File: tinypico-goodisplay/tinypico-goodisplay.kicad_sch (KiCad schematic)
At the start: 23 parts, among them Q1 Si1308, U1 TinypicoESP32_Symbol

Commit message: Update C4
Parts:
- U2: value (none) -> FPCConn; footprint (none) -> footprint:Hirose_FH12-24S-0.5SH_1x24-1MP_P0.50mm_Horizontal
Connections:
- net GND: no longer U2.MP (26)
- net VCOM: now reaches C1.2, U2.1 (24)
- net VCOM: now also U1.5 (IO4)
- no-connect marks 11 -> 12
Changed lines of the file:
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@@
   (junction (at 60.96 101.6) (diameter 0) (color 0 0 0 0)
   )
+  (junction (at 59.69 99.06) (diameter 0) (color 0 0 0 0)
+  )
   (junction (at 77.47 80.01) (diameter 0) (color 0 0 0 0)
   )
@@
   (junction (at 82.55 87.63) (diameter 0) (color 0 0 0 0)
   )
-  (no_connect (at 227.33 95.25))
+  (no_connect (at 52.07 96.52))
   (no_connect (at 199.39 95.25))
   (no_connect (at 227.33 110.49))
   (no_connect (at 199.39 99.06))
+  (no_connect (at 49.53 160.02))
   (no_connect (at 227.33 80.01))
   (no_connect (at 227.33 102.87))
@@
     (stroke (width 0) (type default) (color 0 0 0 0))
   )
-  (wire (pts (xy 52.07 160.02) (xy 52.07 161.29))
-    (stroke (width 0) (type default) (color 0 0 0 0))
-  )
   (wire (pts (xy 78.74 111.76) (xy 58.42 111.76))
     (stroke (width 0) (type default) (color 0 0 0 0))
@@
     (stroke (width 0) (type default) (color 0 0 0 0))
   )
+  (wire (pts (xy 59.69 96.52) (xy 59.69 99.06))
+    (stroke (width 0) (type default) (color 0 0 0 0))
+  )
+  (wire (pts (xy 59.69 99.06) (xy 58.42 99.06))
+    (stroke (width 0) (type default) (color 0 0 0 0))
+  )
   (wire (pts (xy 110.49 143.51) (xy 110.49 146.05))
     (stroke (width 0) (type default) (color 0 0 0 0))
@@
     (stroke (width 0) (type default) (color 0 0 0 0))
   )
-  (wire (pts (xy 52.07 96.52) (xy 52.07 95.25))
-    (stroke (width 0) (type default) (color 0 0 0 0))
-  )
   (wire (pts (xy 101.6 158.75) (xy 85.09 158.75))
     (stroke (width 0) (type default) (color 0 0 0 0))
@@
     (stroke (width 0) (type default) (color 0 0 0 0))
   )
-  (wire (pts (xy 69.85 99.06) (xy 58.42 99.06))
+  (wire (pts (xy 69.85 99.06) (xy 59.69 99.06))
     (stroke (width 0) (type default) (color 0 0 0 0))
   )
@@
     (stroke (width 0) (type default) (color 0 0 0 0))
   )
-  (wire (pts (xy 39.37 95.25) (xy 52.07 95.25))
-    (stroke (width 0) (type default) (color 0 0 0 0))
-  )
   (wire (pts (xy 110.49 158.75) (xy 109.22 158.75))
     (stroke (width 0) (type default) (color 0 0 0 0))
@@
     (stroke (width 0) (type default) (color 0 0 0 0))
   )
+  (wire (pts (xy 227.33 95.25) (xy 236.22 95.25))
+    (stroke (width 0) (type default) (color 0 0 0 0))
+  )
   (wire (pts (xy 191.77 83.82) (xy 199.39 83.82))
     (stroke (width 0) (type default) (color 0 0 0 0))
@@
   )
   (wire (pts (xy 88.9 114.3) (xy 88.9 111.76))
-    (stroke (width 0) (type default) (color 0 0 0 0))
-  )
-  (wire (pts (xy 49.53 160.02) (xy 52.07 160.02))
     (stroke (width 0) (type default) (color 0 0 0 0))
   )
@@
     (effects (font (size 2 2) (thickness 0.4) bold) (justify left bottom))
   )
+  (label "VCOM" (at 59.69 96.52 90)
+    (effects (font (size 1.27 1.27)) (justify left bottom))
+  )
   (label "EPD_RST" (at 106.68 134.62 0)
     (effects (font (size 1.27 1.27)) (justify left bottom))
@@
   (label "EPD_CS" (at 191.77 91.44 180)
     (effects (font (size 1.27 1.27)) (justify right bottom))
+  )
+  (label "VCOM" (at 236.22 95.25 0)
+    (effects (font (size 1.27 1.27)) (justify left bottom))
   )
   (label "EPD_CLK" (at 191.77 87.63 180)
@@
     (pin "1")
   )
-  (symbol (lib_id "power:GND") (at 52.07 161.29 0) (unit 1)
-    (in_bom yes) (on_board yes)
-    (property "Reference" "#PWR0115" (id 0) (at 52.07 167.64 0)
-      (effects (font (size 1.27 1.27)) hide)
-    )
-    (property "Value" "GND" (id 1) (at 52.197 165.6842 0))
-    (property "Footprint" "" (id 2) (at 52.07 161.29 0)
-      (effects (font (size 1.27 1.27)) hide)
-    )
-    (property "Datasheet" "" (id 3) (at 52.07 161.29 0)
-      (effects (font (size 1.27 1.27)) hide)
-    )
-    (pin "1")
-  )
-  (symbol (lib_id "power:GND") (at 39.37 95.25 0) (unit 1)
-    (in_bom yes) (on_board yes)
-    (property "Reference" "#PWR0116" (id 0) (at 39.37 101.6 0)
-      (effects (font (size 1.27 1.27)) hide)
-    )
-    (property "Value" "GND" (id 1) (at 39.497 99.6442 0))
-    (property "Footprint" "" (id 2) (at 39.37 95.25 0)
-      (effects (font (size 1.27 1.27)) hide)
-    )
-    (property "Datasheet" "" (id 3) (at 39.37 95.25 0)
-      (effects (font (size 1.27 1.27)) hide)
-    )
-    (pin "1")
-  )
   (symbol (lib_id "M5StampC3-rescue:FPCConn-Connector2") (at 58.42 153.67 0) (unit 1)
     (in_bom yes) (on_board yes)
@@
       (effects (font (size 1.27 1.27)) (justify right))
     )
-    (property "Value" "" (id 1) (at 45.0342 129.413 0)
+    (property "Value" "FPCConn" (id 1) (at 45.0342 129.413 0)
       (effects (font (size 1.27 1.27)) (justify right))
     )
-    (property "Footprint" "" (id 2) (at 58.42 153.67 0)
+    (property "Footprint" "footprint:Hirose_FH12-24S-0.5SH_1x24-1MP_P0.50mm_Horizontal" (id 2) (at 58.42 153.67 0)
       (effects (font (size 1.27 1.27)) hide)
     )
@@
     (pin "8")
     (pin "9")
-    (pin "MP")
-    (pin "MP")
+    (pin "P2")
+    (pin "P1")
   )
   (symbol (lib_id "power:+3V3") (at 129.54 83.82 0) (unit 1)
@@
       (reference "#PWR0112") (unit 1) (value "GND") (footprint "")
     )
-    (path "/00000000-0000-0000-0000-0000606d480f"
-      (reference "#PWR0115") (unit 1) (value "GND") (footprint "")
-    )
-    (path "/00000000-0000-0000-0000-0000607026b5"
-      (reference "#PWR0116") (unit 1) (value "GND") (footprint "")
-    )
     (path "/00000000-0000-0000-0000-000061a87074"

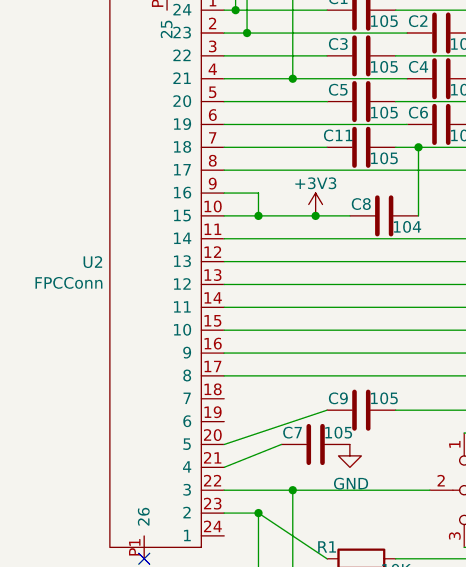
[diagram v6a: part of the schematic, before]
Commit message: Goodisplay FPC connector pins are on the TOP
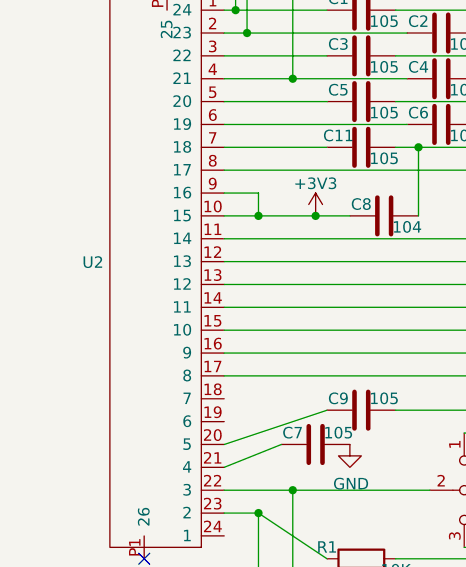
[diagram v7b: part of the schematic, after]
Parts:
- R2: LCSC C247097 -> C25040
- R3: LCSC C247015 -> C247097
- U2: value FPCConn -> (none); footprint footprint:Hirose_FH12-24S-0.5SH_1x24-1MP_P0.50mm_Horizontal -> (none); LCSC C202112 -> C506794
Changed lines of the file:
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@@
       (effects (font (size 1.27 1.27)) (justify right))
     )
-    (property "Value" "FPCConn" (id 1) (at 45.0342 129.413 0)
+    (property "Value" "" (id 1) (at 45.0342 129.413 0)
       (effects (font (size 1.27 1.27)) (justify right))
     )
-    (property "Footprint" "footprint:Hirose_FH12-24S-0.5SH_1x24-1MP_P0.50mm_Horizontal" (id 2) (at 58.42 153.67 0)
+    (property "Footprint" "" (id 2) (at 58.42 153.67 0)
       (effects (font (size 1.27 1.27)) hide)
     )
@@
       (effects (font (size 1.27 1.27)) hide)
     )
-    (property "LCSC" "C202112" (id 4) (at 58.42 153.67 0)
+    (property "LCSC" "C506794" (id 4) (at 58.42 153.67 0)
       (effects (font (size 1.27 1.27)) hide)
     )
@@
     (pin "8")
     (pin "9")
+    (pin "P1")
     (pin "P2")
-    (pin "P1")
   )
   (symbol (lib_id "power:+3V3") (at 129.54 83.82 0) (unit 1)
@@
       (effects (font (size 1.27 1.27)) hide)
     )
-    (property "LCSC" "C247097" (id 4) (at 105.41 146.05 90)
+    (property "LCSC" "C25040" (id 4) (at 105.41 146.05 90)
       (effects (font (size 1.27 1.27)) hide)
     )
@@
       (effects (font (size 1.27 1.27)) hide)
     )
-    (property "LCSC" "C247015" (id 4) (at 105.41 158.75 90)
-      (effects (font (size 1.27 1.27)) hide)
-    )
+    (property "LCSC" "C247097" (id 4) (at 105.41 158.75 90)
+      (effects (font (size 1.27 1.27)) hide)
+    )

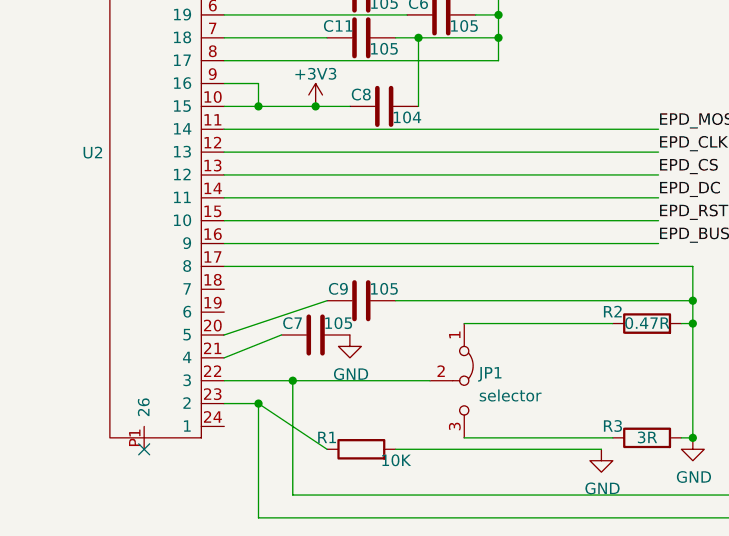
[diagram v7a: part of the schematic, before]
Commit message: Add RES switch
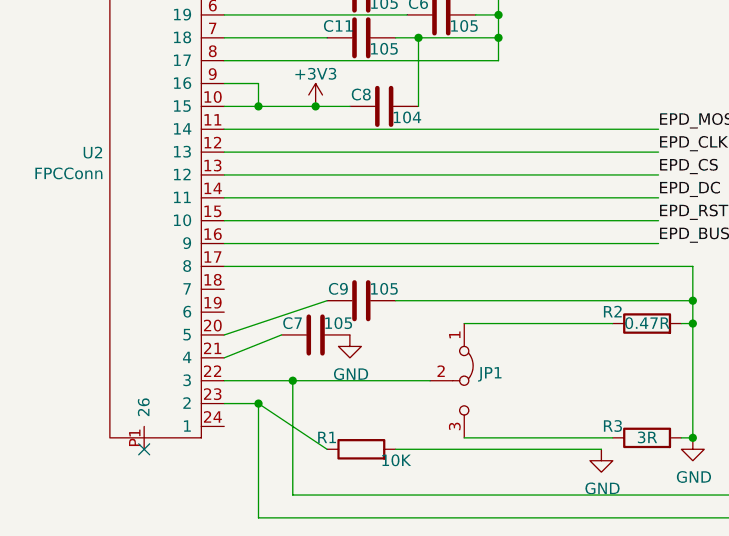
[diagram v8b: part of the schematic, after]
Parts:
- JP1: value selector -> (none); footprint Jumper:SolderJumper-3_P1.3mm_Open_Pad1.0x1.5mm -> (none); LCSC (none) -> C2911519
- U2: value (none) -> FPCConn; footprint (none) -> footprint:Hirose_FH12-24S-0.5SH_1x24-1MP_P0.50mm_Horizontal
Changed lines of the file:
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@@
       (effects (font (size 1.27 1.27)) (justify right))
     )
-    (property "Value" "" (id 1) (at 45.0342 129.413 0)
+    (property "Value" "FPCConn" (id 1) (at 45.0342 129.413 0)
       (effects (font (size 1.27 1.27)) (justify right))
     )
-    (property "Footprint" "" (id 2) (at 58.42 153.67 0)
+    (property "Footprint" "footprint:Hirose_FH12-24S-0.5SH_1x24-1MP_P0.50mm_Horizontal" (id 2) (at 58.42 153.67 0)
       (effects (font (size 1.27 1.27)) hide)
     )
@@
       (effects (font (size 1.27 1.27)) (justify left))
     )
-    (property "Value" "selector" (id 1) (at 86.7162 154.1022 90)
+    (property "Value" "" (id 1) (at 86.7162 154.1022 90)
       (effects (font (size 1.27 1.27)) (justify left))
     )
-    (property "Footprint" "Jumper:SolderJumper-3_P1.3mm_Open_Pad1.0x1.5mm" (id 2) (at 85.09 152.4 0)
+    (property "Footprint" "" (id 2) (at 85.09 152.4 0)
       (effects (font (size 1.27 1.27)) hide)
     )
     (property "Datasheet" "~" (id 3) (at 85.09 152.4 0)
+      (effects (font (size 1.27 1.27)) hide)
+    )
+    (property "LCSC" "C2911519" (id 4) (at 85.09 152.4 90)
       (effects (font (size 1.27 1.27)) hide)
     )
@@
     )
     (path "/3a6b8f9d-0005-44a5-95a4-3e58bdf1c3ef"
-      (reference "JP1") (unit 1) (value "selector") (footprint "Jumper:SolderJumper-3_P1.3mm_Open_Pad1.0x1.5mm")
+      (reference "JP1") (unit 1) (value "selector") (footprint "footprint:switch-MK-12C02-G020")
     )
     (path "/00000000-0000-0000-0000-0000606b755b"
